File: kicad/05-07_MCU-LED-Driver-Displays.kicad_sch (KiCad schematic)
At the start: 73 parts, among them J4 Conn_02x05_Counter_Clockwise, J5 Conn_01x02_Pin, J6 Conn_01x03_Pin, J7 Conn_01x03_Pin, J9 Conn_01x12_Pin, Q4 AO3400A, Q5 AO3400A, SW1 BOOTSEL, SW2 RESET, SW3 USER_A, SW4 USER_B_PWR, SW5 B3U-1100PM, U5 W25Q128JVS, U6 PCF8523T, U7 RP2040, Y1 ABS07AIG-32.768KHZ-7-T, Y2 ABM8-272-T3

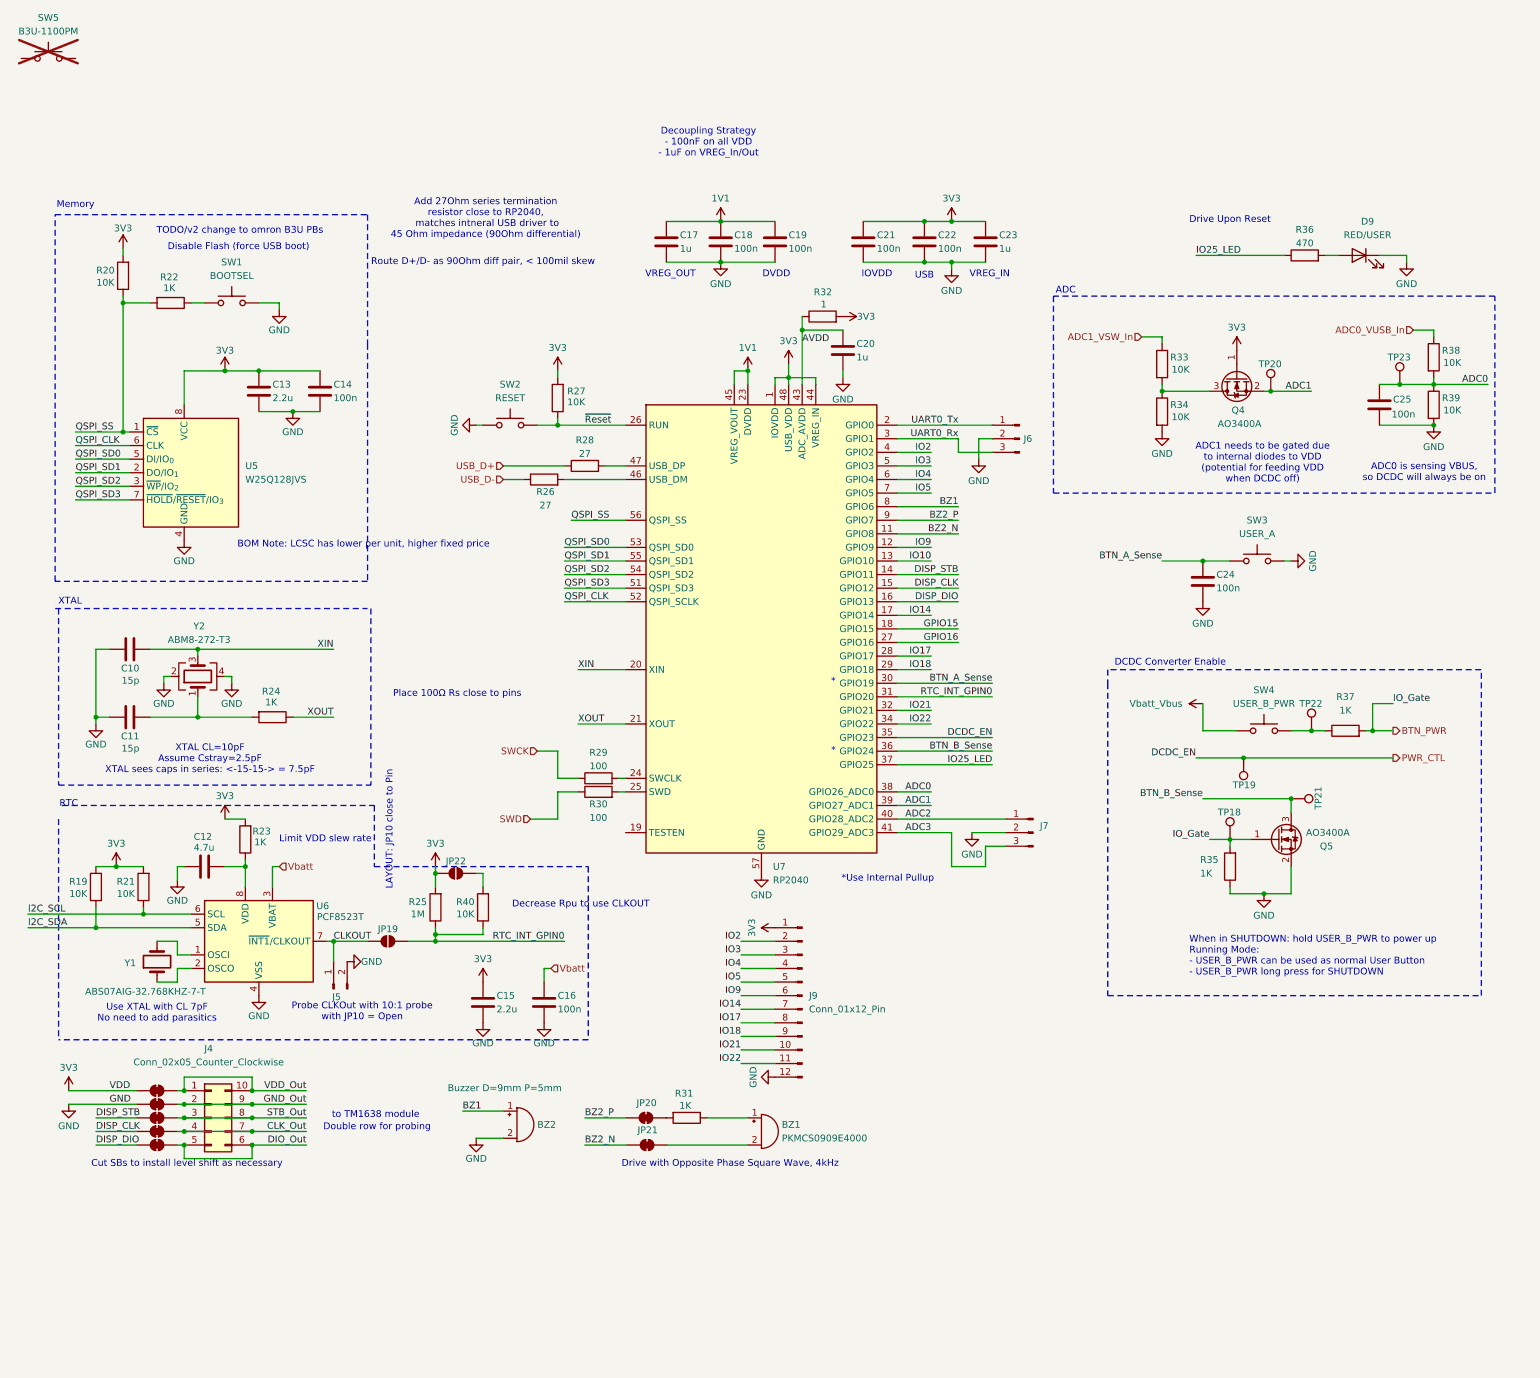
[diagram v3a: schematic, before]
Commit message: rtc new sheet, pullups
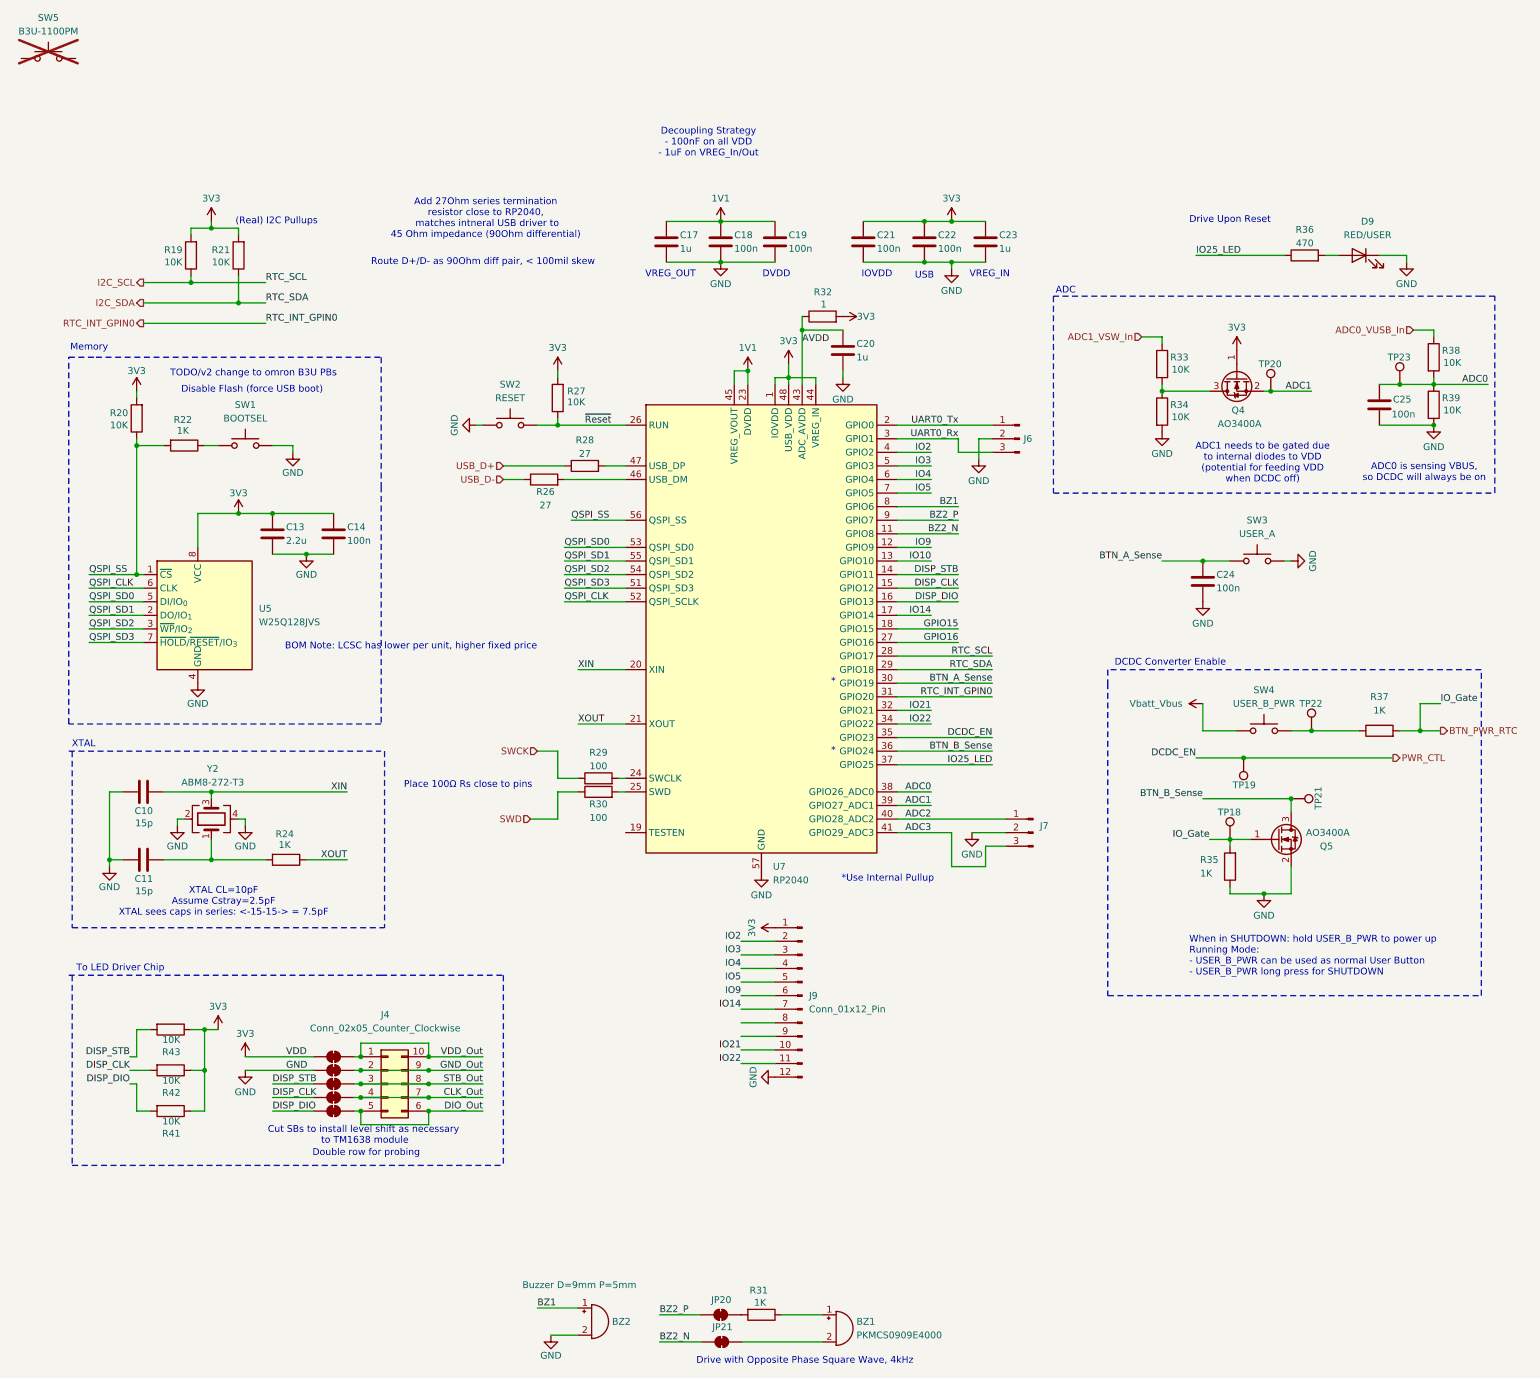
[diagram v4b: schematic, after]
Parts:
- removed C12: 4.7u, symbol Device:C
- removed C15: 2.2u, symbol Device:C
- removed C16: 100n, symbol Device:C
- removed J5: Conn_01x02_Pin, symbol Connector:Conn_01x02_Pin
- removed JP19, JP22: SolderJumper_2_Open, Jumper:SolderJumper-2_P1.3mm_Open_RoundedPad1.0x1.5mm, symbol Jumper:SolderJumper_2_Open
- removed R23: 1K, Resistor_SMD:R_0805_2012Metric_Pad1.20x1.40mm_HandSolder, symbol Device:R
- removed R25: 1M, Resistor_SMD:R_0805_2012Metric_Pad1.20x1.40mm_HandSolder, symbol Device:R
- removed R40: 10K, Resistor_SMD:R_0805_2012Metric_Pad1.20x1.40mm_HandSolder, symbol Device:R
- removed U6: PCF8523T, Package_SO:SOIC-8_3.9x4.9mm_P1.27mm, symbol Timer_RTC:PCF8523T
- removed Y1: ABS07AIG-32.768KHZ-7-T, symbol Device:Crystal
- added R41, R42, R43: 10K, Resistor_SMD:R_0805_2012Metric_Pad1.20x1.40mm_HandSolder, symbol Device:R
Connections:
- net 3V3: now also R41.1, R42.1, R43.1
- net DISP_CLK: now also R42.2
- net DISP_DIO: now also R41.2
- net DISP_STB: now also R43.2
- net I2C_SCL: now also R19.1, U7.28 (GPIO17); no longer R21.1
- net I2C_SDA: now also R21.1, U7.29 (GPIO18); no longer R19.1
- net BTN_PWR renamed BTN_PWR_RTC
- net IO17: no longer names the net of J9.8 (Pin_8)
- net IO17: no longer U7.28 (GPIO17)
- net IO18: no longer names the net of J9.9 (Pin_9)
- net IO18: no longer U7.29 (GPIO18)
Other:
- note added: "(Real) I2C Pullups"
- note added: "To LED Driver Chip"
- note removed: "Decrease Rpu to use CLKOUT"
- note removed: "LAYOUT: JP10 close to Pin"
- note removed: "Limit VDD slew rate"
- note removed: "Probe CLKOut with 10:1 probe with JP10 = Open"
- note removed: "RTC"
- note removed: "Use XTAL with CL 7pF No need to add parasitics"
- moved on the sheet: BZ1, BZ2, C10, C11, C13, C14, J4, JP20, JP21, R19, R20, R21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

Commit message: pre ERC
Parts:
- J5: renamed from J4; footprint (none) -> Connector_PinHeader_2.54mm:PinHeader_2x05_P2.54mm_Vertical; Subsystem (none) -> 06-MCU-IO
- R20: renamed from R43; Manufacturer (none) -> (Generic); Package (none) -> 0805; Subsystem (none) -> 06-MCU-IO; Supplier 1 (none) -> (Generic)
- R21: renamed from R42; Manufacturer (none) -> (Generic); Package (none) -> 0805; Subsystem (none) -> 06-MCU-IO; Supplier 1 (none) -> (Generic)
- R22: renamed from R41; Manufacturer (none) -> (Generic); Package (none) -> 0805; Subsystem (none) -> 06-MCU-IO; Supplier 1 (none) -> (Generic)
- R24: renamed from R19; Manufacturer (none) -> (Generic); Package (none) -> 0805; Subsystem (none) -> 06-MCU-IO; Supplier 1 (none) -> (Generic)
- R25: renamed from R21; Manufacturer (none) -> (Generic); Package (none) -> 0805; Subsystem (none) -> 06-MCU-IO; Supplier 1 (none) -> (Generic)
- R27: renamed from R26; Manufacturer (none) -> (Generic); Package (none) -> 0805; Subsystem (none) -> 06-MCU-IO; Supplier 1 (none) -> (Generic)
- R29: renamed from R28; Manufacturer (none) -> (Generic); Package (none) -> 0805; Subsystem (none) -> 06-MCU-IO; Supplier 1 (none) -> (Generic)
- R32: renamed from R31; Manufacturer (none) -> (Generic); Supplier 1 (none) -> (Generic)
- R34: renamed from R33; Manufacturer (none) -> (Generic); Supplier 1 (none) -> (Generic)
- R35: renamed from R34; Manufacturer (none) -> (Generic); Supplier 1 (none) -> (Generic)
- R36: renamed from R35; Manufacturer (none) -> (Generic); Supplier 1 (none) -> (Generic)
- R37: renamed from R36; Manufacturer (none) -> (Generic); Supplier 1 (none) -> (Generic)
- R38: renamed from R37; Manufacturer (none) -> (Generic); Supplier 1 (none) -> (Generic)
- R39: renamed from R38; Manufacturer (none) -> (Generic); Supplier 1 (none) -> (Generic)
- R40: renamed from R39; Manufacturer (none) -> (Generic); Supplier 1 (none) -> (Generic)
- TP19: value TestPoint -> DCDC_EN
- TP23: value TestPoint -> ADC0
- renumbered BZ2 to BZ1, BZ1 to BZ2, C13 to C12, C14 to C13, C17 to C14, C18 to C15, C19 to C16, C20 to C17, C21 to C18, C22 to C19, C23 to C20, C24 to C21, C25 to C22, J9 to J6, J6 to J7, J7 to J8, JP20 to JP19, JP21 to JP20, R20 to R19, R22 to R23, R24 to R26, R27 to R28, R29 to R30, R30 to R31, R32 to R33, SW5 to SW1, SW1 to SW2, SW2 to SW3, SW3 to SW4, SW4 to SW5, U7 to U6, Y2 to Y1

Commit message: ERC done
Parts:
- removed J6: Conn_01x12_Pin, Connector_PinHeader_2.54mm:PinHeader_1x12_P2.54mm_Vertical, symbol Connector:Conn_01x12_Pin
- added J6: Conn_01x13_Pin, Connector_PinHeader_2.54mm:PinHeader_1x13_P2.54mm_Vertical, symbol Connector:Conn_01x13_Pin
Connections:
- net 3V3: now also J6.1 (Pin_1)
- net GND: now also U6.19 (TESTEN), J6.13 (Pin_13)
- net IO10: now also J6.7 (Pin_7)
- net IO14: now also J6.8 (Pin_8)
- net IO2: now also J6.2 (Pin_2)
- net IO21: now also J6.11 (Pin_11)
- net IO22: now also J6.12 (Pin_12)
- net IO3: now also J6.3 (Pin_3)
- net IO4: now also J6.4 (Pin_4)
- net IO5: now also J6.5 (Pin_5)
- net IO9: now also J6.6 (Pin_6)
- net GPIO15 renamed IO15
- net IO15: now also J6.9 (Pin_9)
- net GPIO16 renamed IO16
- net IO16: now also J6.10 (Pin_10)
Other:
- note added: "I2C for RTC module"
- note removed: "(Real) I2C Pullups"
- moved on the sheet: BZ1, BZ2, JP19, JP20, R32

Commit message: floorplanning
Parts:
- J5: symbol Connector_Generic:Conn_02x05_Counter_Clockwise -> Connector_Generic:Conn_02x05_Odd_Even
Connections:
- net CLK_Out: now also J5.8 (Pin_8); no longer J5.4 (Pin_4)
- net DIO_Out: now also J5.10 (Pin_10), J5.9 (Pin_9); no longer J5.5 (Pin_5), J5.6 (Pin_6)
- net GND_Out: now also J5.3 (Pin_3), J5.4 (Pin_4); no longer J5.2 (Pin_2), J5.9 (Pin_9)
- net STB_Out: now also J5.5 (Pin_5), J5.6 (Pin_6); no longer J5.3 (Pin_3), J5.8 (Pin_8)
- net VDD_Out: now also J5.2 (Pin_2); no longer J5.10 (Pin_10)
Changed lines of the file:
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@@
 	)
 	(symbol
-		(lib_id "Connector_Generic:Conn_02x05_Counter_Clockwise")
+		(lib_id "Connector_Generic:Conn_02x05_Odd_Even")
 		(at 77.47 180.34 0)
 		(unit 1)
@@
 			)
 		)
-		(property "Description" "Generic connector, double row, 02x05, counter clockwise pin numbering scheme (similar to DIP package numbering), script generated (kicad-library-utils/schlib/autogen/connector/)"
+		(property "Description" "Generic connector, double row, 02x05, odd/even pin numbering scheme (row 1 odd numbers, row 2 even numbers), script generated (kicad-library-utils/schlib/autogen/connector/)"
 			(at 77.47 180.34 0)
 			(effects

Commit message: buzzer fp, power mux layout
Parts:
- BZ1: footprint project footprints:Buz-TH_D9.6_P5 -> project footprints:Buzzer-TH_D9.6_P5
- BZ2: footprint project footprints:SPKR_PKMCS0909E4000-R1 -> project footprints:Buzzer_SPKR_PKMCS0909E4000-R1
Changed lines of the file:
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@@
 			)
 		)
-		(property "Footprint" "project footprints:SPKR_PKMCS0909E4000-R1"
+		(property "Footprint" "project footprints:Buzzer_SPKR_PKMCS0909E4000-R1"
 			(at 173.355 161.29 90)
 			(effects
@@
 			)
 		)
-		(property "Footprint" "project footprints:Buz-TH_D9.6_P5"
+		(property "Footprint" "project footprints:Buzzer-TH_D9.6_P5"
 			(at 161.925 181.61 90)
 			(effects
